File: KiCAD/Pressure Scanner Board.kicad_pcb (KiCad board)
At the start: 2 copper layers, 56 parts, among them J1 Cortex_Debug, J2 USB_Micro_B, J3 Binder 709 Female Panel Mount, Q1 3.7A, 30V, Q2 BSS138, Q3 BSS138, SW1 FSMCTTR, U1 SAMD21G18A-AU, U10 DLHR-L10D-E1BD-C-NAV8, U11 DLHR-L10D-E1BD-C-NAV8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

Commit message: More layout
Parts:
- moved U11 165.7 mm to (186.2, 128.8), turned to 180 degrees
- moved D1 146.6 mm to (119.9, 84.2), turned to 180 degrees
- moved U7 133.1 mm to (165.2, 128.8), turned to 180 degrees
- moved Y2 114.2 mm to (137.0, 113.5)
- moved R2 109.7 mm to (136.4, 78.0), turned to 180 degrees
- moved U9 105.8 mm to (144.2, 128.8), turned to 180 degrees
- moved U4 99.0 mm to (209.0, 106.0), turned to 90 degrees
- moved Q3 98.1 mm to (165.5, 114.5)
- moved C18 95.9 mm to (142.5, 113.0)
- moved U6 92.9 mm to (123.2, 128.8), turned to 180 degrees
- moved C16 90.1 mm to (132.0, 112.5), turned to 90 degrees
- moved R10 89.5 mm to (155.5, 96.5), turned to 270 degrees
- moved R6 83.5 mm to (160.0, 108.0), turned to 270 degrees
- moved C15 79.0 mm to (150.5, 93.0), turned to 270 degrees
- moved R1 77.5 mm to (185.4, 106.3), turned to 90 degrees
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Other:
- board text added: "To-Do: 1. Mark differential pairs in eeschema for routing"

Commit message: Bit more layout, prepping to start routing soon
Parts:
- U10, U11, U12, U4, U5, U6, U7, U8, U9: moved to B.Cu
- moved U4 23.5 mm to (187.2, 97.2)
- moved R1 8.59 mm to (177.5, 103.0)
- moved C7 6.36 mm to (172.0, 104.0), turned to 180 degrees
- moved J1 5.54 mm to (186.8, 84.8)
- moved C3 2.11 mm to (176.0, 97.0)
- moved C4 2.11 mm to (180.0, 97.0)
- moved C5 1.58 mm to (159.5, 86.0)
- moved C6 1.58 mm to (156.0, 81.9)
- moved L1 1.58 mm to (162.5, 79.4)
- moved SW1 1.28 mm to (187.2, 97.6)
- turned U10 to 180 degrees
- turned U11 to 0 degrees
- turned U12 to 180 degrees
- turned U5 to 180 degrees
- turned U6 to 0 degrees
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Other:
- board text added: "To-Do: 1. Mark differential pairs in eeschema for routing 2. Check size of static pressure sensor"
- board text removed: "To-Do: 1. Mark differential pairs in eeschema for routing"

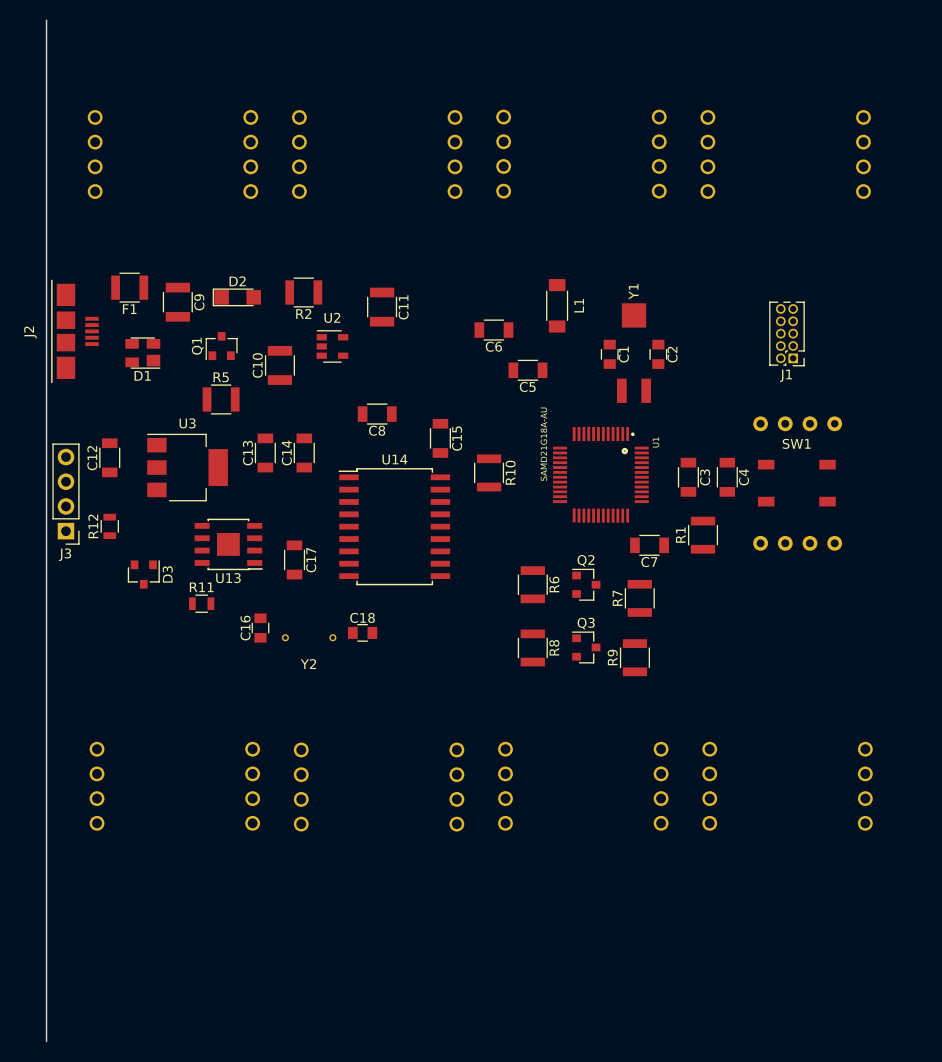
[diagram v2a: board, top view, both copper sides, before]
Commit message: Began routing, added differential pair labels
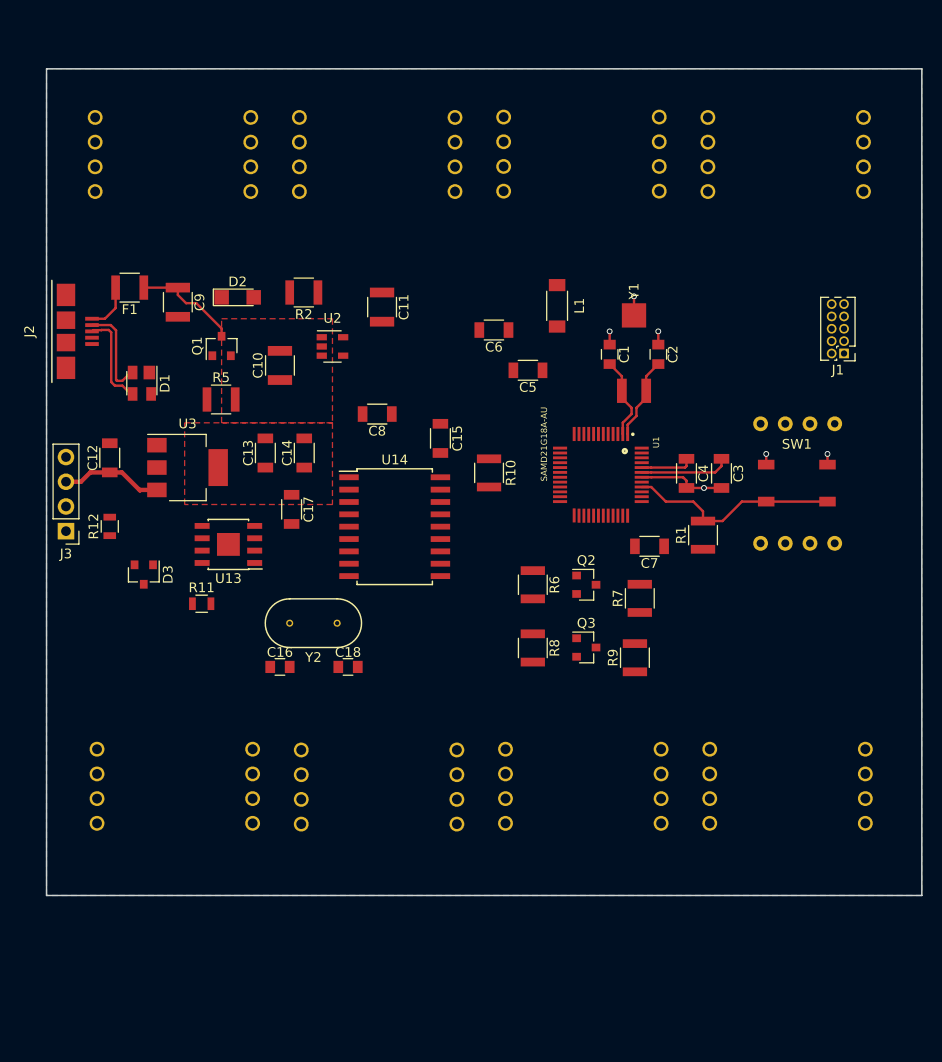
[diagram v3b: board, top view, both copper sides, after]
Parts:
- moved J1 5.25 mm to (192.0, 84.3)
- moved C17 5.21 mm to (135.2, 100.3)
- moved C16 4.47 mm to (134.0, 116.5), turned to 0 degrees
- moved C4 4.22 mm to (175.8, 96.6)
- moved C18 3.81 mm to (141.0, 116.5)
- moved C3 3.42 mm to (179.4, 96.6)
- moved D1 3.10 mm to (119.8, 87.3), turned to 270 degrees
- moved Y2 1.56 mm to (137.4, 112.0)
- moved C7 0.10 mm to (172.0, 104.1)
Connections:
- net Net-(C1-Pad2) renamed /OSC-
- net Net-(C16-Pad2) renamed /CAN Bus/OSC+
- net Net-(C18-Pad1) renamed /CAN Bus/OSC-
- net Net-(C2-Pad2) renamed /OSC+
- C17 pad 1: +3V3 -> +5V
- F1 pad 2: Net-(F1-Pad2) -> VBUS
- J2 pad 1: Net-(F1-Pad2) -> VBUS
- U13 pad 3: +3V3 -> +5V
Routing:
- net RESETN: track 0.00 -> 22.0 mm
- net GND: track 0.00 -> 16.0 mm, vias 0 -> 6
- net Net-(C9-Pad1): track 0.00 -> 11.0 mm
- net +BATT: track 0.00 -> 10.5 mm
- net USB_D+: track 0.00 -> 9.96 mm
- net USB_D-: track 0.00 -> 9.89 mm
- net Net-(C3-Pad1): track 0.00 -> 9.22 mm
- net /OSC+: track 0.00 -> 8.50 mm
- net /OSC-: track 0.00 -> 8.50 mm
- net +3V3: track 0.00 -> 5.41 mm
- net VBUS: track 0.00 -> 4.98 mm
- added copper zone on F.Cu, net +5V
- added copper zone on B.Cu, net GND
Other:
- board outline added: 90 x 85 mm

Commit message: More Layout
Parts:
- moved R12 110.5 mm to (225.8, 85.9), turned to 0 degrees
- moved D3 103.4 mm to (221.3, 86.8), turned to 180 degrees
- moved U13 96.1 mm to (224.4, 95.5), turned to 90 degrees
- moved R11 94.0 mm to (218.3, 92.7), turned to 270 degrees
- moved C17 90.2 mm to (225.4, 102.4), turned to 180 degrees
- moved J3 87.5 mm to (197.1, 82.2)
- moved U14 81.3 mm to (226.4, 112.6), turned to 270 degrees
- moved C16 79.4 mm to (211.8, 100.8), turned to 270 degrees
- moved Y2 79.3 mm to (216.3, 104.2), turned to 270 degrees
- moved C12 77.3 mm to (192.3, 79.8), turned to 270 degrees
- moved C18 71.4 mm to (211.8, 107.8), turned to 270 degrees
- moved C15 68.1 mm to (216.2, 111.2), turned to 180 degrees
- moved R10 62.4 mm to (214.9, 115.5), turned to 180 degrees
- moved U3 62.4 mm to (184.8, 79.8), turned to 180 degrees
- moved C13 46.2 mm to (176.8, 81.2), turned to 270 degrees
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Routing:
- net RESETN: track 22.0 -> 8.34 mm
- net Net-(C9-Pad1): track 11.0 -> 0.00 mm
- net +BATT: track 10.5 -> 0.00 mm
- net GND: track 16.0 -> 9.09 mm, vias 6 -> 1
- net VBUS: track 4.98 -> 0.00 mm
- net USB_D+: track 9.96 -> 8.74 mm
- net USB_D-: track 9.89 -> 9.00 mm
- removed copper zone on F.Cu, net +5V
- removed copper zone on B.Cu, net GND

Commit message: Redoing layout
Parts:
- added J4: Can Header, Pin_Headers:Pin_Header_Straight_1x02_Pitch2.54mm, F.Cu at (155.0, 150.1)
- J3: value Binder 709 Female Panel Mount -> Battery Headers; footprint Pin_Headers:Pin_Header_Straight_1x04_Pitch2.54mm -> Pin_Headers:Pin_Header_Straight_1x02_Pitch2.54mm
- moved D2 102.6 mm to (192.1, 105.1), turned to 180 degrees
- moved J2 96.4 mm to (195.8, 34.3), turned to 90 degrees
- moved R2 91.2 mm to (185.8, 105.1), turned to 0 degrees
- moved J3 84.4 mm to (112.7, 84.7), turned to 0 degrees
- moved C12 82.2 mm to (121.7, 37.7), turned to 90 degrees
- moved D1 79.6 mm to (183.4, 31.4), turned to 180 degrees
- moved F1 73.5 mm to (184.6, 37.9), turned to 0 degrees
- moved U3 69.6 mm to (129.3, 37.7), turned to 0 degrees
- moved C9 61.2 mm to (176.6, 37.6), turned to 90 degrees
- moved C13 58.6 mm to (139.3, 36.2), turned to 90 degrees
- moved R5 57.8 mm to (168.5, 34.6), turned to 180 degrees
- moved C14 52.9 mm to (145.0, 36.2), turned to 90 degrees
- moved C10 51.0 mm to (160.8, 36.6), turned to 90 degrees
- moved Q1 49.3 mm to (167.9, 39.1), turned to 270 degrees
- moved C11 46.6 mm to (152.6, 31.9), turned to 180 degrees
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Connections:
- net RX_LED renamed Net-(U1-Pad48)
- net TX_LED renamed Net-(U1-Pad39)
- D3 pad 1: CANH -> /CAN Bus/+
- D3 pad 2: CANL -> /CAN Bus/-
- J3 pad 1: CANH -> +BATT
- J3 pad 2: CANL -> GND
- R12 pad 1: CANH -> /CAN Bus/+
- R12 pad 2: CANL -> /CAN Bus/-
- U13 pad 6: CANL -> /CAN Bus/-
- U13 pad 7: CANH -> /CAN Bus/+
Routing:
- net RESETN: track 8.34 -> 20.6 mm
- net USB_D-: track 9.00 -> 0.00 mm
- net USB_D+: track 8.74 -> 0.01 mm
- net GND: track 9.09 -> 5.07 mm, vias 1 -> 0
- net +3V3: track 5.41 -> 6.57 mm
- net Net-(C3-Pad1): track 9.22 -> 10.2 mm

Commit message: More Routing
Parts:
- U13: footprint Housings_SOIC:SOIC-8-1EP_3.9x4.9mm_Pitch1.27mm -> Housings_SOIC:SOIC-8_3.9x4.9mm_Pitch1.27mm
- moved R12 105.4 mm to (118.2, 108.7), turned to 90 degrees
- moved D3 101.3 mm to (119.1, 114.0), turned to 270 degrees
- moved U13 94.9 mm to (125.9, 108.6), turned to 180 degrees
- moved C17 93.7 mm to (127.3, 104.2)
- moved U5 90.5 mm to (123.1, 128.9), turned to 0 degrees
- moved U6 90.3 mm to (186.0, 63.8), turned to 180 degrees
- moved R11 89.9 mm to (126.0, 112.4), turned to 0 degrees
- moved C16 86.4 mm to (123.3, 121.5), turned to 0 degrees
- moved Y2 86.1 mm to (126.7, 117.3), turned to 0 degrees
- moved U14 84.2 mm to (137.8, 109.5), turned to 0 degrees
- moved C18 78.3 mm to (130.2, 121.5), turned to 0 degrees
- moved C15 74.0 mm to (137.9, 116.8)
- moved R10 72.9 mm to (139.2, 101.6)
- moved J4 58.7 mm to (112.2, 110.0), turned to 180 degrees
- moved C9 56.7 mm to (181.8, 94.0), turned to 270 degrees
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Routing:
- net MOSI_0: track 0.00 -> 129.6 mm, vias 0 -> 4
- net SCLK_0: track 0.00 -> 104.9 mm, vias 0 -> 4
- net GND: track 5.07 -> 106.5 mm, vias 0 -> 20
- net SS_1: track 0.00 -> 82.2 mm, vias 0 -> 8
- net SS_3: track 0.00 -> 81.9 mm, vias 0 -> 4
- net MISO_0: track 0.00 -> 66.2 mm
- net USB_D-: track 0.00 -> 64.0 mm, vias 0 -> 4
- net USB_D+: track 0.01 -> 59.0 mm, vias 0 -> 2
- net SS_0: track 0.00 -> 51.2 mm, vias 0 -> 6
- net SS_2: track 0.00 -> 44.4 mm, vias 0 -> 4
- net +3V3: track 6.57 -> 44.9 mm, vias 0 -> 4
- net +5V: track 0.00 -> 37.2 mm
- net RESETN: track 20.6 -> 47.1 mm, vias 0 -> 2
- net SCL_L: track 0.00 -> 22.0 mm
- net SDA_L: track 0.00 -> 19.4 mm
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- added copper zone on F.Cu, net +3V3
- added copper zone on F.Cu, net +5V
- added copper zone on B.Cu, net GND

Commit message: More route
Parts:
- added  : Via, Via, F.Cu at (136.0, 97.0)
- added  : Via, Via, F.Cu at (138.5, 94.5)
- added  : Via, Via, F.Cu at (136.0, 94.5)
- added  : Via, Via, F.Cu at (138.5, 92.0)
- added  : Via, Via, F.Cu at (136.0, 92.0)
- added  : Via, Via, F.Cu at (138.5, 89.5)
- added  : Via, Via, F.Cu at (136.0, 89.5)
- added  : Via, Via, F.Cu at (138.5, 87.0)
- added  : Via, Via, F.Cu at (136.0, 87.0)
- moved C16 1.09 mm to (123.0, 120.5)
- moved C18 1.07 mm to (130.0, 120.5)
- moved Y2 0.88 mm to (126.5, 116.5)
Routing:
- net +5V: track 37.2 -> 66.8 mm, vias 0 -> 4
- net GND: track 106.5 -> 123.5 mm, vias 20 -> 28
- net +3V3: track 44.9 -> 50.3 mm, vias 4 -> 5
- net /CAN Bus/OSC-: track 12.4 -> 15.4 mm
- net /CAN Bus/OSC+: track 15.3 -> 16.5 mm
- added copper zone on B.Cu, net +3V3
- added copper zone on B.Cu, net +5V
- added copper zone on F.Cu, net GND

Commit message: Reset the routing
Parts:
- moved U13 8.19 mm to (119.5, 103.5)
- moved R12 2.82 mm to (121.0, 109.0)
- moved C17 2.70 mm to (127.5, 101.5)
- moved U1 1.03 mm to (154.0, 99.0)
- moved Y1 0.24 mm to (156.5, 87.0)
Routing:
- net MOSI_0: track 129.6 -> 0.00 mm, vias 4 -> 0
- net GND: track 123.5 -> 0.00 mm, vias 28 -> 0
- net SCLK_0: track 104.9 -> 0.00 mm, vias 4 -> 0
- net SS_1: track 82.2 -> 0.00 mm, vias 8 -> 0
- net SS_3: track 81.9 -> 0.00 mm, vias 4 -> 0
- net +5V: track 66.8 -> 0.00 mm, vias 4 -> 0
- net MISO_0: track 66.2 -> 0.00 mm
- net USB_D-: track 64.0 -> 0.00 mm, vias 4 -> 0
- net USB_D+: track 59.0 -> 0.00 mm, vias 2 -> 0
- net SS_0: track 51.2 -> 0.00 mm, vias 6 -> 0
- net +3V3: track 50.3 -> 0.00 mm, vias 5 -> 0
- net RESETN: track 47.1 -> 0.00 mm, vias 2 -> 0
- net SS_2: track 44.4 -> 0.00 mm, vias 4 -> 0
- net SCL_L: track 22.0 -> 0.00 mm
- net SDA_L: track 19.4 -> 0.00 mm
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- removed copper zone on B.Cu, net +3V3
- removed copper zone on F.Cu, net +3V3
- removed copper zone on B.Cu, net +5V
- removed copper zone on F.Cu, net +5V
- removed copper zone on B.Cu, net GND
- removed copper zone on F.Cu, net GND
